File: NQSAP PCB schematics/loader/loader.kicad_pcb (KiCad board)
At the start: 2 copper layers, 102 x 96 mm, 19 parts, among them J1 Bus, J2 Bus, J5 Conn_02x08, SW1 RESET, U1 74LS173, U2 74LS173, U3 74HCT574, U4 74HCT574, U5 74HCT00

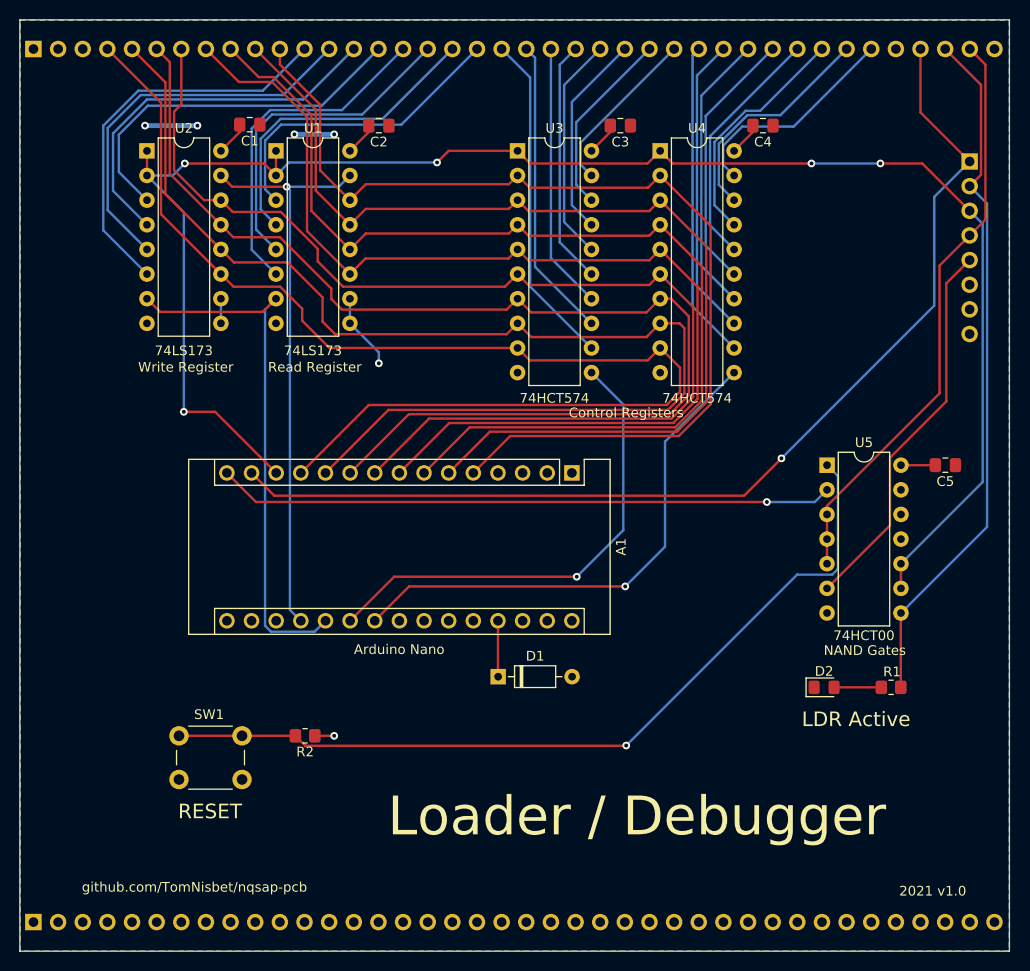
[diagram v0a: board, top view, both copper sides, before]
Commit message: Add Microcode and IR/RC modules.  Add clock circuit to Loader module.
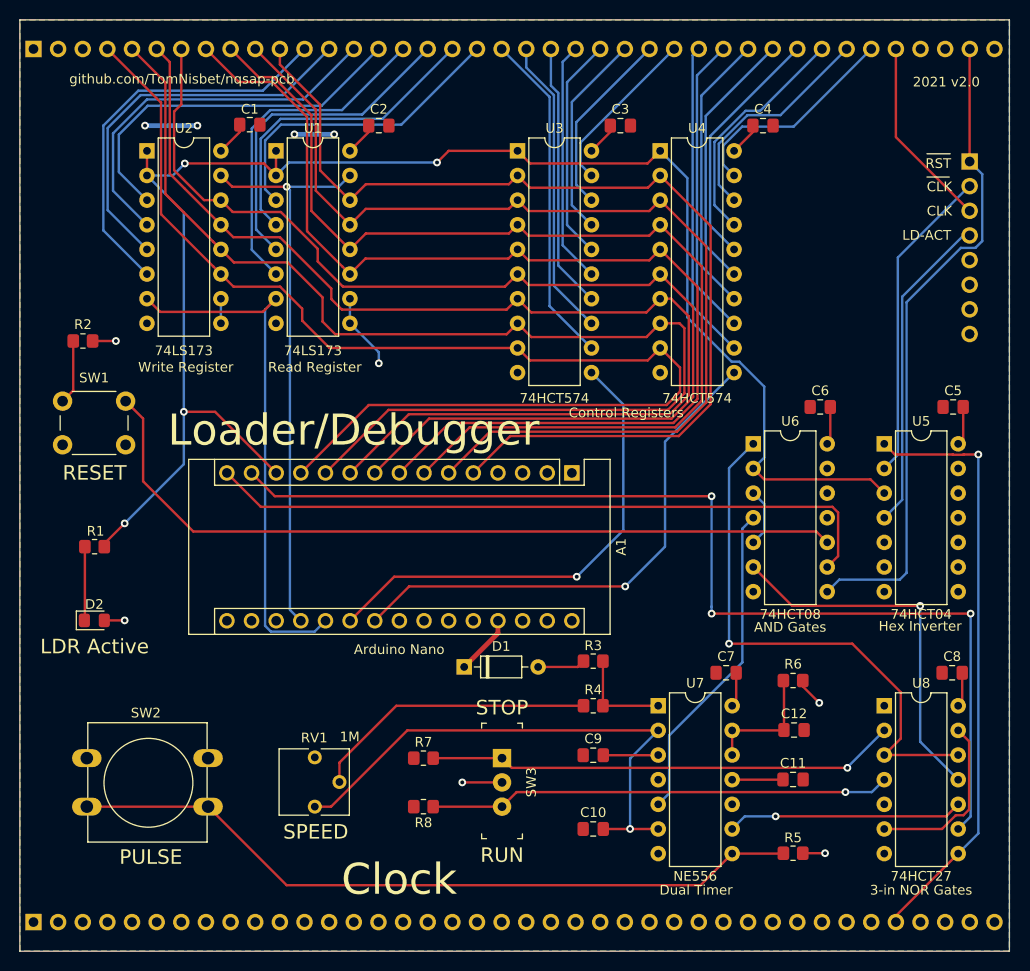
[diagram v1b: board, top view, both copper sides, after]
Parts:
- added C10: 1uF, Capacitor_SMD:C_0805_2012Metric_Pad1.18x1.45mm_HandSolder, F.Cu at (144.1, 126.4)
- added C11: 0.01uF, Capacitor_SMD:C_0805_2012Metric_Pad1.18x1.45mm_HandSolder, F.Cu at (164.7, 121.3)
- added C12: 0.1uF, Capacitor_SMD:C_0805_2012Metric_Pad1.18x1.45mm_HandSolder, F.Cu at (164.8, 116.2)
- added C6: 0.1uF, Capacitor_SMD:C_0805_2012Metric_Pad1.18x1.45mm_HandSolder, F.Cu at (167.5, 82.9)
- added C7: 0.1uF, Capacitor_SMD:C_0805_2012Metric_Pad1.18x1.45mm_HandSolder, F.Cu at (157.8, 110.3)
- added C8: 0.1uF, Capacitor_SMD:C_0805_2012Metric_Pad1.18x1.45mm_HandSolder, F.Cu at (181.1, 110.3)
- added C9: 0.01uF, Capacitor_SMD:C_0805_2012Metric_Pad1.18x1.45mm_HandSolder, F.Cu at (144.1, 118.8)
- added R3: 1K, Resistor_SMD:R_0805_2012Metric_Pad1.20x1.40mm_HandSolder, F.Cu at (144.1, 109.1)
- added R4: 1K, Resistor_SMD:R_0805_2012Metric_Pad1.20x1.40mm_HandSolder, F.Cu at (144.1, 113.7)
- added R5: 1K, Resistor_SMD:R_0805_2012Metric_Pad1.20x1.40mm_HandSolder, F.Cu at (164.7, 128.9)
- added R6: 1M, Resistor_SMD:R_0805_2012Metric_Pad1.20x1.40mm_HandSolder, F.Cu at (164.7, 111.1)
- added R7: 1K, Resistor_SMD:R_0805_2012Metric_Pad1.20x1.40mm_HandSolder, F.Cu at (126.6, 119.1)
- added R8: 1K, Resistor_SMD:R_0805_2012Metric_Pad1.20x1.40mm_HandSolder, F.Cu at (126.6, 124.1)
- added RV1: 1M, Potentiometer_THT:Potentiometer_Vishay_T73YP_Vertical, F.Cu at (115.4, 124.1)
- added SW2: PULSE, Button_Switch_THT:SW_PUSH-12mm, F.Cu at (91.9, 119.1)
- added SW3: RUN, digikey-footprints:Switch_Slide_11.6x4mm_EG1218, F.Cu at (134.7, 119.1)
- added U6: 74HCT08, Package_DIP:DIP-14_W7.62mm, F.Cu at (160.6, 86.7)
- added U7: NE556, Package_DIP:DIP-14_W7.62mm, F.Cu at (150.8, 113.7)
- added U8: 74HCT27, Package_DIP:DIP-14_W7.62mm, F.Cu at (174.1, 113.7)
- R1: value 100 -> R-BLUE
- SW1: footprint Button_Switch_THT:SW_PUSH_6mm_H7.3mm -> Button_Switch_THT:SW_PUSH_6mm
- U5: value 74HCT00 -> 74HCT04
- moved R1 83.4 mm to (92.7, 97.3)
- moved D2 75.5 mm to (92.7, 104.9)
- moved R2 46.7 mm to (91.5, 76.1)
- moved SW1 36.5 mm to (95.9, 86.8)
- moved U5 6.30 mm to (174.1, 86.7)
- moved C5 6.05 mm to (181.2, 82.9), turned to 0 degrees
- moved D1 3.64 mm to (130.8, 109.7)
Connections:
- net NC-1 renamed Net-(J1-Pad3)
- net NC-2 renamed Net-(J1-Pad2)
- A1 pad 13: ~LDR-ACT -> ~LD-ACT
- A1 pad 14: LDR-CLK -> LD-CLK
- C1 pad 2: +5V -> VCC
- C2 pad 2: +5V -> VCC
- C3 pad 2: +5V -> VCC
- C4 pad 2: +5V -> VCC
- C5 pad 2: +5V -> VCC
- D1 pad 2: +5V -> VCC
- D2 pad 1: GND -> Net-(D2-Pad1)
- D2 pad 2: Net-(D2-Pad2) -> VCC
- J1 pad 37: LDR-CLK -> Net-(J1-Pad37)
- J1 pad 38: LDR-ACT -> Net-(J1-Pad38)
- J1 pad 39: RST -> ~RST
- J1 pad 40: +5V -> VCC
- J2 pad 36: Net-(J2-Pad36) -> CLK
- J2 pad 40: +5V -> VCC
- J5 pad 1: LDR-CLK -> ~RST
- J5 pad 2: LDR-ACT -> ~CLK
- J5 pad 3: ~LDR-ACT -> CLK
- J5 pad 4: RST -> LD-ACT
- J5 pad 5: ~RST -> Net-(J5-Pad5)
- R1 pad 1: LDR-ACT -> ~LD-ACT
- R1 pad 2: Net-(D2-Pad2) -> Net-(D2-Pad1)
- R2 pad 1: +5V -> VCC
- U1 pad 1: ~LDR-ACT -> ~LD-ACT
- U1 pad 16: +5V -> VCC
- U1 pad 2: ~LDR-ACT -> ~LD-ACT
- U2 pad 1: ~LDR-ACT -> ~LD-ACT
- U2 pad 16: +5V -> VCC
- U2 pad 2: ~LDR-ACT -> ~LD-ACT
- U3 pad 1: ~LDR-ACT -> ~LD-ACT
- U3 pad 20: +5V -> VCC
- U4 pad 1: ~LDR-ACT -> ~LD-ACT
- U4 pad 20: +5V -> VCC
- U5 pad 1: /~BT-R -> CLK
- U5 pad 10: ~LDR-ACT -> Net-(U5-Pad10)
- U5 pad 11: Net-(U5-Pad11) -> GND
- U5 pad 12: +5V -> Net-(U5-Pad12)
- U5 pad 13: +5V -> GND
- U5 pad 14: +5V -> VCC
- U5 pad 2: /~LD-R -> ~CLK
- U5 pad 3: RST -> ~LD-ACT
- U5 pad 4: RST -> LD-ACT
- U5 pad 5: RST -> GND
- U5 pad 6: ~RST -> Net-(U5-Pad6)
- U5 pad 8: LDR-ACT -> Net-(U5-Pad8)
- U5 pad 9: ~LDR-ACT -> GND
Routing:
- net ~LDR-ACT: track 176.6 -> 0.00 mm, vias 5 -> 0
- net ~LD-ACT: track 0.00 -> 169.2 mm, vias 0 -> 4
- net LD-CLK: track 0.00 -> 109.9 mm, vias 0 -> 3
- net LDR-CLK: track 109.5 -> 0.00 mm, vias 1 -> 0
- net CLK: track 0.00 -> 81.7 mm, vias 0 -> 1
- net Net-(R5-Pad2): track 0.00 -> 76.5 mm
- net LDR-ACT: track 71.8 -> 0.00 mm
- net RST: track 60.5 -> 0.00 mm
- net run-~stop: track 0.00 -> 56.2 mm, vias 0 -> 1
- net Net-(C10-Pad1): track 0.00 -> 55.7 mm, vias 0 -> 1
- net Net-(R7-Pad2): track 0.00 -> 48.8 mm, vias 0 -> 1
- net Net-(R8-Pad1): track 0.00 -> 47.7 mm, vias 0 -> 1
- net VCC: track 0.00 -> 47.6 mm, vias 0 -> 5
- net Net-(U6-Pad6): track 0.00 -> 38.4 mm, vias 0 -> 1
- net astable: track 0.00 -> 33.6 mm
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- added copper zone on B.Cu, net VCC
- removed copper zone on B.Cu, net +5V
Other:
- board text added: "2021 v2.0"
- board text added: "CLK"
- board text added: "Clock"
- board text added: "LD-ACT"
- board text added: "Loader/Debugger"
- board text added: "RST"
- board text removed: "2021 v1.0"
- board text removed: "Loader / Debugger"

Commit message: Add RAM, update and add gerbers for new boards
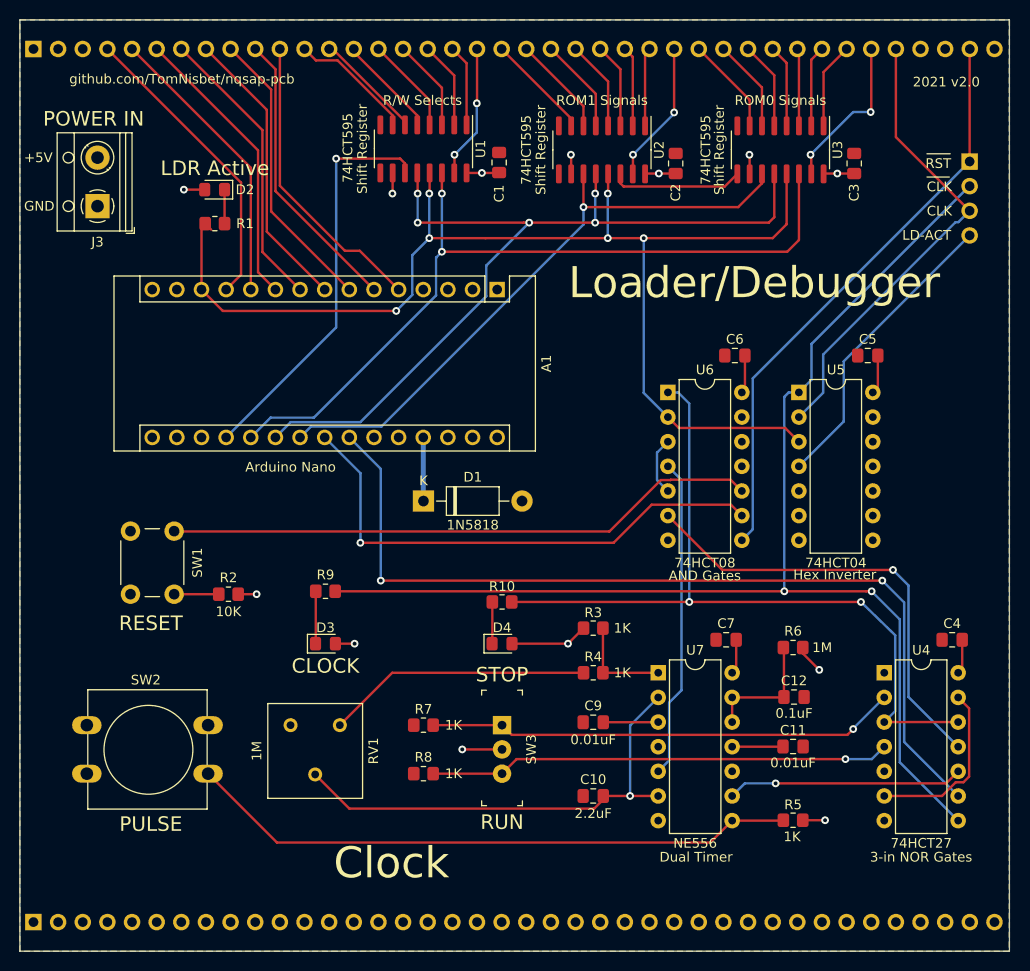
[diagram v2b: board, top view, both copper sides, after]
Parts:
- removed C8: 0.1uF, Capacitor_SMD:C_0805_2012Metric_Pad1.18x1.45mm_HandSolder
- removed the U4 at (151.0, 56.5)
- added D3: CLOCK, LED_SMD:LED_0805_2012Metric_Pad1.15x1.40mm_HandSolder, F.Cu at (116.5, 107.3)
- added D4: STOP, LED_SMD:LED_0805_2012Metric_Pad1.15x1.40mm_HandSolder, F.Cu at (134.7, 107.3)
- added J3: POWER IN, TerminalBlock_RND:TerminalBlock_RND_205-00012_1x02_P5.00mm_Horizontal, F.Cu at (93.0, 62.2)
- added R10: R-RED, Resistor_SMD:R_0805_2012Metric_Pad1.20x1.40mm_HandSolder, F.Cu at (134.7, 103.0)
- added R9: R-BLUE, Resistor_SMD:R_0805_2012Metric_Pad1.20x1.40mm_HandSolder, F.Cu at (116.5, 101.9)
- C10: value 1uF -> 2.2uF
- D1: value diode -> 1N5818; footprint Diode_THT:D_DO-35_SOD27_P7.62mm_Horizontal -> Diode_THT:D_DO-41_SOD81_P10.16mm_Horizontal
- J5: value Conn_02x08 -> IB-TR; footprint Connector_PinHeader_2.54mm:PinHeader_1x08_P2.54mm_Vertical -> Connector_PinHeader_2.54mm:PinHeader_1x04_P2.54mm_Vertical
- RV1: footprint Potentiometer_THT:Potentiometer_Vishay_T73YP_Vertical -> Potentiometer_THT:Potentiometer_Bourns_3386F_Vertical
- U1, U2: value 74LS173 -> 74HCT595; footprint Package_DIP:DIP-16_W7.62mm -> Package_SO:SOIC-16_3.9x9.9mm_P1.27mm
- U3: value 74HCT574 -> 74HCT595; footprint Package_DIP:DIP-20_W7.62mm -> Package_SO:SOIC-16_3.9x9.9mm_P1.27mm
- moved C4 56.5 mm to (181.1, 106.9), turned to 0 degrees
- moved U2 46.9 mm to (145.0, 56.4), turned to 270 degrees
- moved D2 46.1 mm to (105.1, 60.5), turned to 180 degrees
- moved R1 35.5 mm to (105.1, 64.0), turned to 0 degrees
- moved C2 30.8 mm to (152.6, 57.8), turned to 270 degrees
- moved R2 30.1 mm to (106.5, 102.2)
- moved U3 27.1 mm to (163.4, 56.4), turned to 270 degrees
- moved C1 26.0 mm to (134.4, 57.7), turned to 270 degrees
- moved C3 24.4 mm to (171.0, 57.8), turned to 270 degrees
- moved A1 20.4 mm to (134.2, 70.8)
- moved D1 17.6 mm to (126.6, 92.6)
- moved SW1 15.4 mm to (96.4, 102.2), turned to 90 degrees
- moved U1 15.2 mm to (126.6, 56.3), turned to 270 degrees
- moved C6 10.3 mm to (158.7, 77.6)
- moved C5 10.3 mm to (172.4, 77.6)
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- renumbered U8 to U4
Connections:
- A1 pad 14: LD-CLK -> Net-(A1-Pad14)
- A1 pad 15: /~LD-R -> Net-(A1-Pad15)
- A1 pad 19: /CLR -> /LD2
- A1 pad 20: /LD2 -> /SER
- A1 pad 21: /LD1 -> /RCLK
- A1 pad 23: Net-(A1-Pad23) -> /~LD-R
- A1 pad 24: Net-(A1-Pad24) -> LD-CLK
- J2 pad 36: CLK -> Net-(J2-Pad36)
- RV1 pad 1: Net-(C10-Pad1) -> Net-(RV1-Pad1)
- RV1 pad 2: Net-(R4-Pad1) -> Net-(C10-Pad1)
- RV1 pad 3: Net-(RV1-Pad3) -> Net-(R4-Pad1)
- U1 pad 1: ~LD-ACT -> RR1
- U1 pad 10: GND -> VCC
- U1 pad 11: D3 -> /LD2
- U1 pad 12: D2 -> /RCLK
- U1 pad 13: D1 -> ~LD-ACT
- U1 pad 14: D0 -> /SER
- U1 pad 15: /CLR -> RR0
- U1 pad 2: ~LD-ACT -> RR2
- U1 pad 3: RR0 -> RR3
- U1 pad 4: RR1 -> WR0
- U1 pad 5: RR2 -> WR1
- U1 pad 6: RR3 -> WR2
- U1 pad 7: /LD2 -> WR3
- U1 pad 9: GND -> Net-(U1-Pad9)
- U2 pad 1: ~LD-ACT -> C1
- U2 pad 10: GND -> VCC
- U2 pad 11: D7 -> /LD0
- U2 pad 12: D6 -> /RCLK
- U2 pad 13: D5 -> ~LD-ACT
- U2 pad 14: D4 -> Net-(U2-Pad14)
- U2 pad 15: /CLR -> C0
- U2 pad 2: ~LD-ACT -> XX0
- U2 pad 3: WR0 -> FB
- U2 pad 4: WR1 -> FC
- U2 pad 5: WR2 -> FZ
- U2 pad 6: WR3 -> FV
- U2 pad 7: /LD2 -> FN
- U2 pad 9: GND -> Net-(U2-Pad9)
- U3 pad 1: ~LD-ACT -> N
- U3 pad 10: GND -> VCC
- U3 pad 11: /LD1 -> /LD0
- U3 pad 12: FN -> /RCLK
- U3 pad 13: FV -> ~LD-ACT
- U3 pad 14: FZ -> /SER
- U3 pad 15: FC -> PI
- U3 pad 16: FB -> VCC
- U3 pad 2: D0 -> JE
- U3 pad 3: D1 -> LF
- U3 pad 4: D2 -> SE
- U3 pad 5: D3 -> SI
- U3 pad 6: D4 -> CC
- U3 pad 7: D5 -> CS
- U3 pad 8: D6 -> GND
- U3 pad 9: D7 -> Net-(U2-Pad14)
- U4 pad 8: CLK -> ~CLK
- U5 pad 1: CLK -> ~CLK
- U5 pad 2: ~CLK -> CLK
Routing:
- net ~CLK: track 32.8 -> 133.2 mm, vias 0 -> 2
- net D6: track 126.3 -> 29.9 mm
- net D7: track 126.8 -> 31.1 mm
- net D5: track 122.1 -> 29.9 mm
- net D4: track 120.3 -> 29.9 mm
- net /RCLK: track 0.00 -> 88.8 mm, vias 0 -> 5
- net D3: track 116.4 -> 29.9 mm
- net D2: track 112.2 -> 29.9 mm
- net /SER: track 0.00 -> 82.2 mm, vias 0 -> 2
- net D1: track 108.5 -> 29.9 mm
- net D0: track 105.8 -> 30.8 mm
- net /CLR: track 59.6 -> 0.00 mm, vias 1 -> 0
- net /LD1: track 49.6 -> 0.00 mm, vias 1 -> 0
- net ~LD-ACT: track 169.2 -> 127.8 mm, vias 4 -> 6
- net CLK: track 81.7 -> 48.5 mm, vias 1 -> 0
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
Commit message: build 5 board updates
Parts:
- added J4: CLK Select, Connector_PinHeader_2.54mm:PinHeader_1x03_P2.54mm_Vertical, F.Cu at (181.7, 86.7)
- moved C5 2.50 mm to (169.9, 77.6)
- moved C6 2.30 mm to (156.4, 77.6)
- moved U5 2.00 mm to (163.3, 81.4)
- moved U6 2.00 mm to (149.8, 81.4)
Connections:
- U6 pad 4: astable -> Net-(J4-Pad2)
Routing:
- net Net-(J4-Pad2): track 0.00 -> 34.9 mm, vias 0 -> 1
- net astable: track 33.0 -> 53.0 mm, vias 0 -> 1
- net /~BT-R: track 65.8 -> 63.8 mm
- net ~RST: track 60.4 -> 62.4 mm
- net /~LD-R: track 53.8 -> 51.8 mm
- net Net-(U4-Pad11): track 46.5 -> 48.5 mm
- net ~LD-ACT: track 127.8 -> 128.8 mm
- net LD-ACT: track 31.1 -> 31.9 mm
- net CLK: track 48.5 -> 49.2 mm
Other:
- board text added: "2021 v2.1"
- board text added: "Use jumper for internal clock"
- board text removed: "2021 v2.0"
